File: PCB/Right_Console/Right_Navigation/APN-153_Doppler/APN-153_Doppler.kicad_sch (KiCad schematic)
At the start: 33 parts, among them J1 J_MCU, J2 J_DOPPLER_SEL, J3 J_MEM_BUTTON, J4 J_BACKLIGHT, Q1 2N7002, SW1 DOPPLER_SEL, U1 MCP23017x-x-SS, U2 DRV8833PWP, U3 ER_OLEDM0.91_1x-I2C

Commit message: feat(pcb): label LCSC/tolerance/voltage on Right_Nav + PDU schematics
Populate LCSC, Tolerance, and Rating (voltage/power) fields across the four
fabbed boards, sourced from InvenTree + the board tickets and PDU DESIGN-NOTES.
Values corrected to the selected part (100nF 50V, resistors 1%, AMS1117
C6186 -> C347222, 10uF split 25V/35V by +12V rail).

- PDU: dividers 0.1% (C2828767/C865184/C406725/C110774), J1 Mini-Fit 4-pin
  C20608114, D3/D4 green, C9 35V on +12V (SMBJ12A clamp margin).
- ARC-51A: MCP23017 C506653, TCA9548 C130026, J9 XH-8 C23067548, backlight
  J8 Mini-Fit 2-pin C20608113.
- ASN-41: AMS1117 C347222, TCA9548 C130026, 10uF per-rail split, 74HC165 x4
  C22384789, 1k ADC filter C844939, backlight J8 C20608113.
- APN-153: footprints (0805 passives + XH/Mini-Fit connectors) + MCP23017
  C506653, DRV8833 C50506, 2N7002 C8545, 2.2uF C87994 (25V X5R), 10nF C1710,
  6-pin XH J2 C23067546.

Off-board panel controls (encoders, rotary switches, OLED, pot, stepper, MEM
button) excluded as connector-coupled. Pin headers (SWD, CAN_TERM) hand-
soldered, no assembly LCSC. Harness mating ends tracked in the order BOM.
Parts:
- C1, C3, C7: footprint (none) -> Capacitor_SMD:C_0805_2012Metric; LCSC (none) -> C1711; Rating (none) -> 50V; Tolerance (none) -> 10%
- C2, C4: footprint (none) -> Capacitor_SMD:C_0805_2012Metric; LCSC (none) -> C669099; Rating (none) -> 25V; Tolerance (none) -> 20%
- C5: footprint (none) -> Capacitor_SMD:C_0805_2012Metric; LCSC (none) -> C87994; Rating (none) -> 25V; Tolerance (none) -> 10%
- C6: footprint (none) -> Capacitor_SMD:C_0805_2012Metric; LCSC (none) -> C1710; Rating (none) -> 50V; Tolerance (none) -> 10%
- D1, D2: footprint (none) -> OpenSkyhawk:LED_5050_Red
- J1: footprint (none) -> Connector_JST:JST_XH_B8B-XH-A_1x08_P2.50mm_Vertical; LCSC (none) -> C23067548
- J2: footprint (none) -> Connector_JST:JST_XH_B6B-XH-A_1x06_P2.50mm_Vertical; LCSC (none) -> C23067546
- J4: footprint (none) -> Connector_Molex:Molex_Mini-Fit_Jr_5566-04A2_2x02_P4.20mm_Vertical; LCSC (none) -> C20608114
- Q1: LCSC (none) -> C8545; Rating (none) -> 60V
- R1, R2: footprint (none) -> Resistor_SMD:R_0805_2012Metric; LCSC (none) -> C2090807; Rating (none) -> 1/8W; Tolerance (none) -> 1%
- R10, R11, R12, R5, R6, R7, R8, R9: footprint (none) -> Resistor_SMD:R_0805_2012Metric; LCSC (none) -> C844937; Rating (none) -> 1/8W; Tolerance (none) -> 1%
- R14: footprint (none) -> Resistor_SMD:R_0805_2012Metric; LCSC (none) -> C844935; Rating (none) -> 1/8W; Tolerance (none) -> 1%
- R15, R3, R4: footprint (none) -> Resistor_SMD:R_0805_2012Metric; LCSC (none) -> C844936; Rating (none) -> 1/8W; Tolerance (none) -> 1%
- U1: LCSC (none) -> C506653
- U2: LCSC (none) -> C50506

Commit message: chore(pcb): normalize passive value-string case fleet-wide
Cosmetic cleanup — standardize resistor/cap value strings so identical
parts stop showing as separate BOM lines. Value = magnitude only;
tolerance + LCSC carry the precision distinction.

- 10K -> 10k, 4.7K -> 4.7k, 100K -> 100k (lowercase SI k)
- 100nf -> 100nF
- 69 symbols across all 6 boards (ASN-41, ARC-51A, APN-153, PDU,
  Gateway_Bridge, PanelGroup_Base). ERC 0/0 on all.

No functional/footprint/LCSC change. PDU generic 10k and precision
divider 10k now both read "10k", distinguished by tolerance (1% vs 0.1%).
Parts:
- R10, R11, R12, R5, R6, R7, R8, R9: value 10K -> 10k
- R14: value 100K -> 100k
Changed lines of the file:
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@@
 			)
 		)
-		(property "Value" "10K"
+		(property "Value" "10k"
 			(at 126.4393 25.3364 90)
 			(show_name no)
@@
 			)
 		)
-		(property "Value" "10K"
+		(property "Value" "10k"
 			(at 123.8993 25.3364 90)
 			(show_name no)
@@
 			)
 		)
-		(property "Value" "10K"
+		(property "Value" "10k"
 			(at 71.1836 60.3993 90)
 			(show_name no)
@@
 			)
 		)
-		(property "Value" "100K"
+		(property "Value" "100k"
 			(at 160.02 148.5899 0)
 			(show_name no)
@@
 			)
 		)
-		(property "Value" "10K"
+		(property "Value" "10k"
 			(at 192.9764 36.1207 90)
 			(show_name no)
@@
 			)
 		)
-		(property "Value" "10K"
+		(property "Value" "10k"
 			(at 111.1993 25.3364 90)
 			(show_name no)
@@
 			)
 		)
-		(property "Value" "10K"
+		(property "Value" "10k"
 			(at 131.5193 25.3364 90)
 			(show_name no)
@@
 			)
 		)
-		(property "Value" "10K"
+		(property "Value" "10k"
 			(at 116.2793 25.3364 90)
 			(show_name no)
@@
 			)
 		)
-		(property "Value" "10K"
+		(property "Value" "10k"
 			(at 118.8193 25.3364 90)
 			(show_name no)

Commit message: refactor(pcb): consolidate ceramic 10uF to single 35V part
The 10uF ceramic 0805 caps were split across two SKUs — C669099 (25V)
and C49010152 (35V) — distinguished only by rail. Standardize all 8
ceramic positions to the 35V part (C49010152); 35V covers the 25V
positions and collapses the BOM to one ceramic 10uF value.

Electrolytic 10uF (C3343) unchanged. Aluminum-bulk replacement deferred
to a future round. 8 caps across all 6 boards, ERC 0/0.
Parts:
- C2, C4: LCSC C669099 -> C49010152; Rating 25V -> 35V
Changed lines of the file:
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@@
 			)
 		)
-		(property "Rating" "25V"
+		(property "Rating" "35V"
 			(at 83.82 25.4 0)
 			(hide yes)
@@
 			)
 		)
-		(property "LCSC" "C669099"
+		(property "LCSC" "C49010152"
 			(at 83.82 25.4 0)
 			(hide yes)
@@
 			)
 		)
-		(property "Rating" "25V"
+		(property "Rating" "35V"
 			(at 238.76 27.94 0)
 			(hide yes)
@@
 			)
 		)
-		(property "LCSC" "C669099"
+		(property "LCSC" "C49010152"
 			(at 238.76 27.94 0)
 			(hide yes)

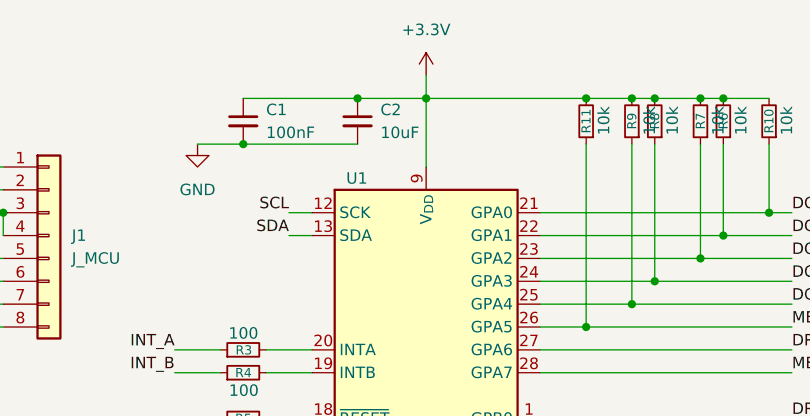
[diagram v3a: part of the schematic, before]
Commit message: fix(pcb): right-size MCP23017/TCA9548 bulk 10uF->1uF (ARC/APN)
The 10uF ceramic bulk beside the MCP23017 and TCA9548 (ARC C2/C20,
APN C2) is oversized: both are low-current I2C parts whose datasheets
call for only 0.1uF, already present. Drop to 1uF (reuse C28323, 0805
unchanged) — keeps ample bulk, frees the 10uF/35V ceramic. No footprint
or symbol change; ERC clean.
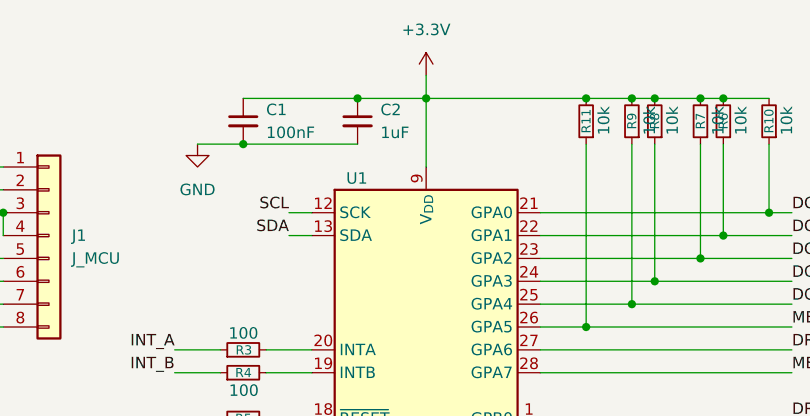
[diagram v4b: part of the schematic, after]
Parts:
- C2: value 10uF -> 1uF; LCSC C49010152 -> C28323; Rating 35V -> 50V; Tolerance 20% -> 10%
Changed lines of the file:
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@@
 			)
 		)
-		(property "Value" "10uF"
+		(property "Value" "1uF"
 			(at 86.36 26.6762 0)
 			(show_name no)
@@
 			)
 		)
-		(property "Rating" "35V"
+		(property "Rating" "50V"
 			(at 83.82 25.4 0)
 			(hide yes)
@@
 			)
 		)
-		(property "Tolerance" "20%"
+		(property "Tolerance" "10%"
 			(at 83.82 25.4 0)
 			(hide yes)
@@
 			)
 		)
-		(property "LCSC" "C49010152"
+		(property "LCSC" "C28323"
 			(at 83.82 25.4 0)
 			(hide yes)
